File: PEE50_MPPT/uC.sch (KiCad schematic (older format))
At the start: 2 parts, among them U4 MSP430FR2353TDBT

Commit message: copy + pasten van schakeling
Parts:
- added J?: Conn_01x03_Female, symbol Connector:Conn_01x03_Female
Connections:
- net GND: now also J?.3 (Pin_3)
- net ADC: now reaches U4.7 (P1-0/UCB0STE/SMCLK/COMP0-0/A0/VEREF+)
- net at U4.8 (TEST/SBWTCK): now also J?.1 (Pin_1)
- net at U4.9 (*RST/NMI/SBWTDIO): now also J?.2 (Pin_2)
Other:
- note added: "RST\n"
- note added: "TEST"
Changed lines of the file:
@@
 $Descr A4 11693 8268
 encoding utf-8
-Sheet 3 5
+Sheet 3 11
 Title ""
 Date ""
@@
 Wire Wire Line
 	7700 4650 7500 4650
+$Comp
+L Connector:Conn_01x03_Female J?
+U 1 1 608C3F1C
+P 8800 2250
+F 0 "J?" H 8827 2276 50  0000 L CNN
+F 1 "Conn_01x03_Female" H 8827 2185 50  0000 L CNN
+F 2 "" H 8800 2250 50  0001 C CNN
+F 3 "~" H 8800 2250 50  0001 C CNN
+	1    8800 2250
+	1    0    0    -1
+$EndComp
+Wire Wire Line
+	7500 2150 8600 2150
+Wire Wire Line
+	8600 2250 7650 2250
+Wire Wire Line
+	7650 2250 7650 1950
+Wire Wire Line
+	7650 1950 3800 1950
+Wire Wire Line
+	3800 1950 3800 2150
+Wire Wire Line
+	3800 2150 3900 2150
+$Comp
+L power:GND #PWR?
+U 1 1 608C4239
+P 8550 2400
+F 0 "#PWR?" H 8550 2150 50  0001 C CNN
+F 1 "GND" H 8555 2227 50  0000 C CNN
+F 2 "" H 8550 2400 50  0001 C CNN
+F 3 "" H 8550 2400 50  0001 C CNN
+	1    8550 2400
+	1    0    0    -1
+$EndComp
+Wire Wire Line
+	8550 2400 8550 2350
+Wire Wire Line
+	8550 2350 8600 2350
+Text Notes 8300 2100 0    50   ~ 0
+TEST
+Text Notes 8300 2350 0    50   ~ 0
+RST\n
+Text HLabel 7650 2300 2    50   Input ~ 0
+ADC
+Wire Wire Line
+	7650 2300 7500 2300
 $EndSCHEMATC

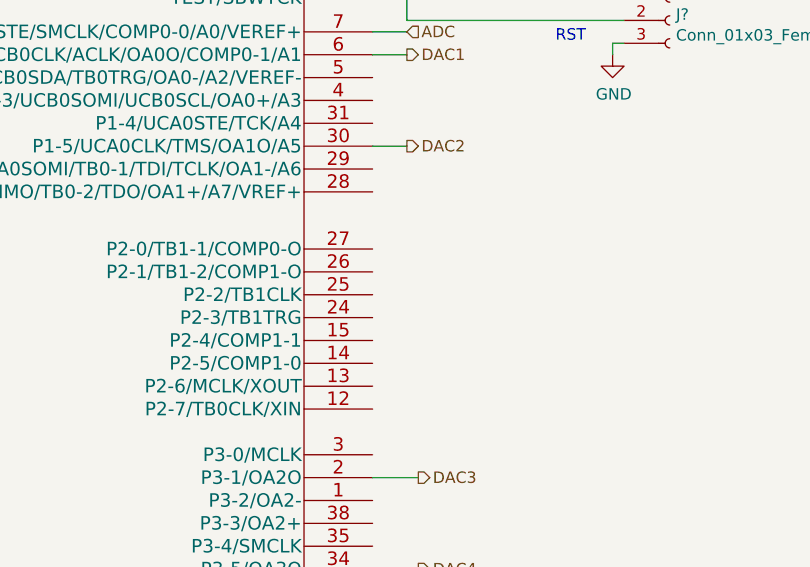
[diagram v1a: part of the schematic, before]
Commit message: mux ingevoegd en geintegreerd
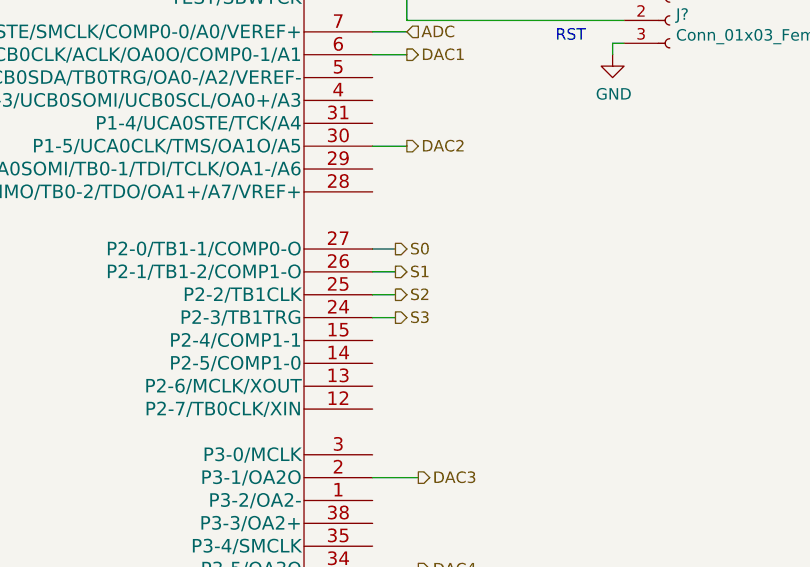
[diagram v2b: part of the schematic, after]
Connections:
- net S3: now reaches U4.24 (P2-3/TB1TRG)
- net S2: now reaches U4.25 (P2-2/TB1CLK)
- net S1: now reaches U4.26 (P2-1/TB1-2/COMP1-O)
- net S0: now reaches U4.27 (P2-0/TB1-1/COMP0-O)
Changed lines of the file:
@@
 $Descr A4 11693 8268
 encoding utf-8
-Sheet 3 11
+Sheet 3 15
 Title ""
 Date ""
@@
 	3800 2150 3900 2150
 $Comp
-L power:GND #PWR?
+L power:GND #PWR0133
 U 1 1 608C4239
 P 8550 2400
-F 0 "#PWR?" H 8550 2150 50  0001 C CNN
+F 0 "#PWR0133" H 8550 2150 50  0001 C CNN
 F 1 "GND" H 8555 2227 50  0000 C CNN
 F 2 "" H 8550 2400 50  0001 C CNN
@@
 Wire Wire Line
 	7650 2300 7500 2300
+Text HLabel 7600 3250 2    50   Output ~ 0
+S0
+Text HLabel 7600 3350 2    50   Output ~ 0
+S1
+Text HLabel 7600 3450 2    50   Output ~ 0
+S2
+Text HLabel 7600 3550 2    50   Output ~ 0
+S3
+Wire Wire Line
+	7500 3550 7600 3550
+Wire Wire Line
+	7500 3450 7600 3450
+Wire Wire Line
+	7500 3350 7600 3350
+Wire Wire Line
+	7500 3250 7600 3250
 $EndSCHEMATC

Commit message: schakeling klaar (denk ik)
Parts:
- added J7: Conn_01x02_Female, symbol Connector:Conn_01x02_Female
- gave numbers to parts that had none: 1
- renumbered C12 to C14, U4 to U5
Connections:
- net at U5.28 (P1-7/UCA0TXD/UCA0SIMO/TB0-2/TDO/OA1+/A7/VREF+): now also J7.2 (Pin_2)
- net at U5.29 (P1-6/UCA0RXD/UCA0SOMI/TB0-1/TDI/TCLK/OA1-/A6): now also J7.1 (Pin_1)
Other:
- note added: "uC RX\nuC TX\n"
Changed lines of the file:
@@
 $EndDescr
 $Comp
-L Robin_lib:MSP430FR2353TDBT U4
+L Robin_lib:MSP430FR2353TDBT U5
 U 1 1 608BCC4E
 P 5700 3600
-F 0 "U4" H 2650 4650 60  0000 C CNN
+F 0 "U5" H 2650 4650 60  0000 C CNN
 F 1 "MSP430FR2353TDBT" H 3050 4750 60  0000 C CNN
 F 2 "DBT38_TEX" H 4950 5250 60  0001 C CNN
@@
 $EndComp
 $Comp
-L power:GND #PWR0111
+L power:GND #PWR028
 U 1 1 608BCC99
 P 5700 5500
-F 0 "#PWR0111" H 5700 5250 50  0001 C CNN
+F 0 "#PWR028" H 5700 5250 50  0001 C CNN
 F 1 "GND" H 5705 5327 50  0000 C CNN
 F 2 "" H 5700 5500 50  0001 C CNN
@@
 	5700 5500 5700 5400
 $Comp
-L Device:C C12
+L Device:C C14
 U 1 1 608BF0BE
 P 5450 1650
-F 0 "C12" V 5198 1650 50  0000 C CNN
+F 0 "C14" V 5198 1650 50  0000 C CNN
 F 1 "C" V 5289 1650 50  0000 C CNN
 F 2 "" H 5488 1500 50  0001 C CNN
@@
 	5700 1650 5700 1800
 $Comp
-L power:GND #PWR0112
+L power:GND #PWR027
 U 1 1 608BF145
 P 5250 1650
-F 0 "#PWR0112" H 5250 1400 50  0001 C CNN
+F 0 "#PWR027" H 5250 1400 50  0001 C CNN
 F 1 "GND" V 5255 1522 50  0000 R CNN
 F 2 "" H 5250 1650 50  0001 C CNN
@@
 	7700 4650 7500 4650
 $Comp
-L Connector:Conn_01x03_Female J?
+L Connector:Conn_01x03_Female J8
 U 1 1 608C3F1C
 P 8800 2250
-F 0 "J?" H 8827 2276 50  0000 L CNN
+F 0 "J8" H 8827 2276 50  0000 L CNN
 F 1 "Conn_01x03_Female" H 8827 2185 50  0000 L CNN
 F 2 "" H 8800 2250 50  0001 C CNN
@@
 	3800 2150 3900 2150
 $Comp
-L power:GND #PWR0133
+L power:GND #PWR029
 U 1 1 608C4239
 P 8550 2400
-F 0 "#PWR0133" H 8550 2150 50  0001 C CNN
+F 0 "#PWR029" H 8550 2150 50  0001 C CNN
 F 1 "GND" H 8555 2227 50  0000 C CNN
 F 2 "" H 8550 2400 50  0001 C CNN
@@
 Wire Wire Line
 	7500 3250 7600 3250
+$Comp
+L Connector:Conn_01x02_Female J7
+U 1 1 6091D58E
+P 7800 2900
+F 0 "J7" H 7827 2876 50  0000 L CNN
+F 1 "Conn_01x02_Female" H 7827 2785 50  0000 L CNN
+F 2 "" H 7800 2900 50  0001 C CNN
+F 3 "~" H 7800 2900 50  0001 C CNN
+	1    7800 2900
+	1    0    0    -1
+$EndComp
+Wire Wire Line
+	7500 2900 7600 2900
+Wire Wire Line
+	7500 3000 7600 3000
+Text Notes 8000 3050 0    50   ~ 0
+uC RX\nuC TX\n
 $EndSCHEMATC

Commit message: best veel footprints ingevoegd
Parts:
- C14: footprint (none) -> Capacitor_SMD:C_1206_3216Metric_Pad1.42x1.75mm_HandSolder
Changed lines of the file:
@@
 EESchema Schematic File Version 4
-LIBS:PEE50_MPPT-cache
-EELAYER 26 0
+EELAYER 30 0
 EELAYER END
 $Descr A4 11693 8268
@@
 F 0 "C14" V 5198 1650 50  0000 C CNN
 F 1 "C" V 5289 1650 50  0000 C CNN
-F 2 "" H 5488 1500 50  0001 C CNN
+F 2 "Capacitor_SMD:C_1206_3216Metric_Pad1.42x1.75mm_HandSolder" H 5488 1500 50  0001 C CNN
 F 3 "~" H 5450 1650 50  0001 C CNN
 	1    5450 1650

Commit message: footprints gemapt + 10x10 pcb rand getekend
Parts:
- J7: footprint (none) -> Connector_PinSocket_2.54mm:PinSocket_1x02_P2.54mm_Vertical
- J8: footprint (none) -> Connector_PinSocket_2.54mm:PinSocket_1x03_P2.54mm_Vertical
- U5: footprint DBT38_TEX -> Robin_Lib:DBT38_TEX
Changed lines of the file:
@@
 EESchema Schematic File Version 4
-EELAYER 30 0
+LIBS:PEE50_MPPT-cache
+EELAYER 26 0
 EELAYER END
 $Descr A4 11693 8268
@@
 F 0 "U5" H 2650 4650 60  0000 C CNN
 F 1 "MSP430FR2353TDBT" H 3050 4750 60  0000 C CNN
-F 2 "DBT38_TEX" H 4950 5250 60  0001 C CNN
+F 2 "Robin_Lib:DBT38_TEX" H 4950 5250 60  0001 C CNN
 F 3 "" H 1600 4400 60  0000 C CNN
 	1    5700 3600
@@
 F 0 "J8" H 8827 2276 50  0000 L CNN
 F 1 "Conn_01x03_Female" H 8827 2185 50  0000 L CNN
-F 2 "" H 8800 2250 50  0001 C CNN
+F 2 "Connector_PinSocket_2.54mm:PinSocket_1x03_P2.54mm_Vertical" H 8800 2250 50  0001 C CNN
 F 3 "~" H 8800 2250 50  0001 C CNN
 	1    8800 2250
@@
 F 0 "J7" H 7827 2876 50  0000 L CNN
 F 1 "Conn_01x02_Female" H 7827 2785 50  0000 L CNN
-F 2 "" H 7800 2900 50  0001 C CNN
+F 2 "Connector_PinSocket_2.54mm:PinSocket_1x02_P2.54mm_Vertical" H 7800 2900 50  0001 C CNN
 F 3 "~" H 7800 2900 50  0001 C CNN
 	1    7800 2900

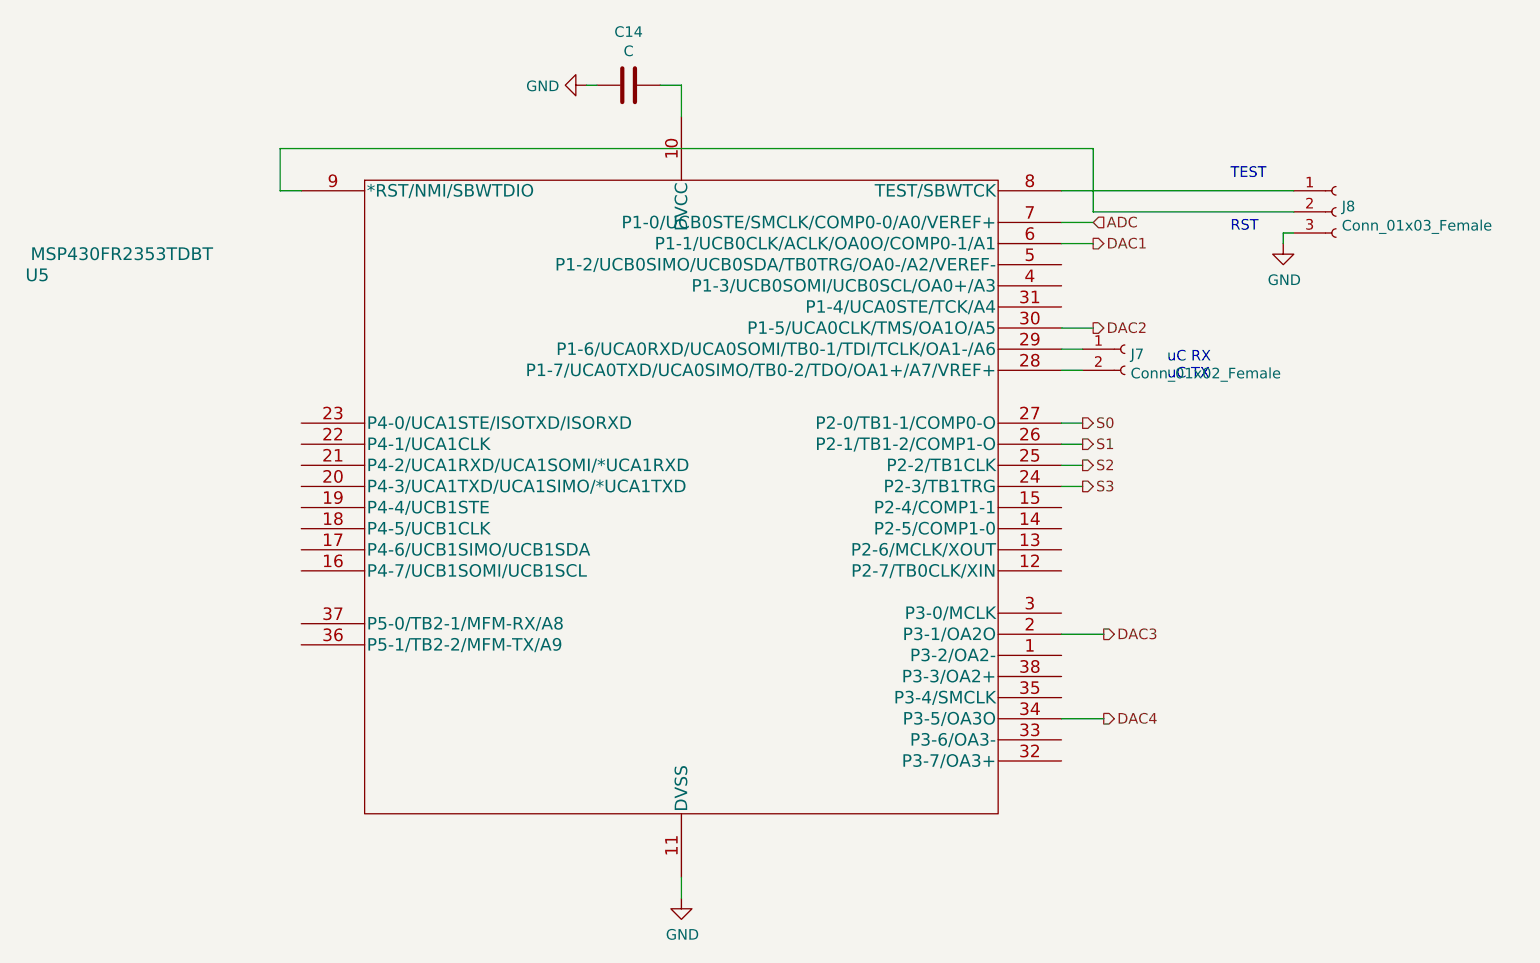
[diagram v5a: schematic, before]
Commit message: maar opnieuw begonnen met mppt layouten ivm plugin regels
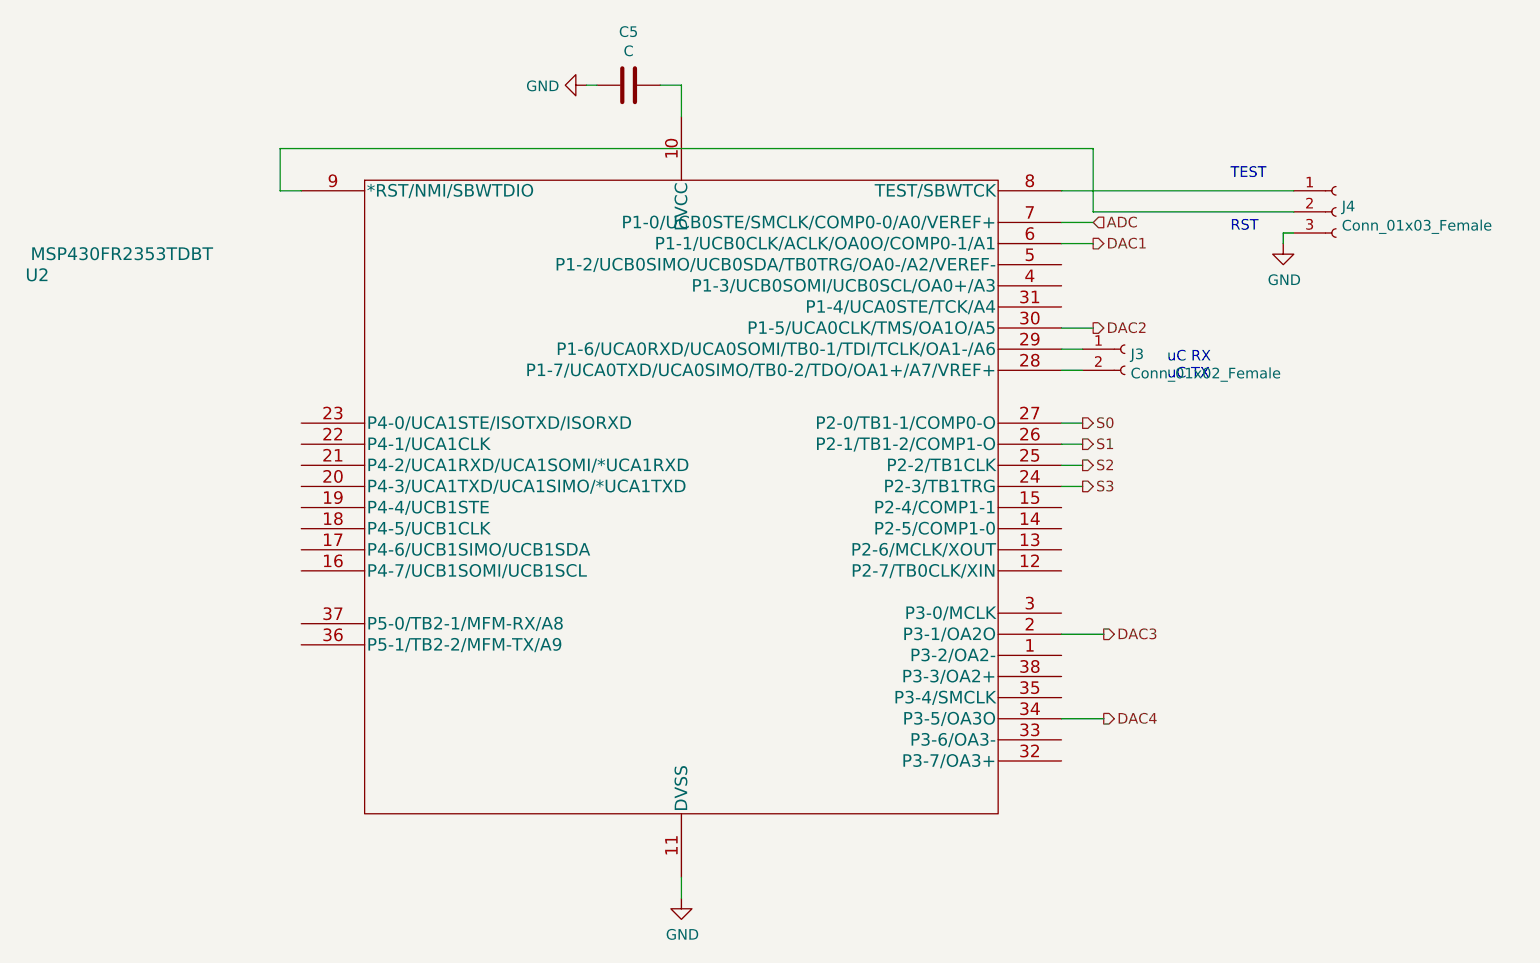
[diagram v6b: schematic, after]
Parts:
- renumbered C14 to C5, J7 to J3, J8 to J4, U5 to U2
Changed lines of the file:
@@
 $Descr A4 11693 8268
 encoding utf-8
-Sheet 3 15
+Sheet 3 19
 Title ""
 Date ""
@@
 $EndDescr
 $Comp
-L Robin_lib:MSP430FR2353TDBT U5
+L Robin_lib:MSP430FR2353TDBT U2
 U 1 1 608BCC4E
 P 5700 3600
-F 0 "U5" H 2650 4650 60  0000 C CNN
+F 0 "U2" H 2650 4650 60  0000 C CNN
 F 1 "MSP430FR2353TDBT" H 3050 4750 60  0000 C CNN
 F 2 "Robin_Lib:DBT38_TEX" H 4950 5250 60  0001 C CNN
@@
 $EndComp
 $Comp
-L power:GND #PWR028
+L power:GND #PWR010
 U 1 1 608BCC99
 P 5700 5500
-F 0 "#PWR028" H 5700 5250 50  0001 C CNN
+F 0 "#PWR010" H 5700 5250 50  0001 C CNN
 F 1 "GND" H 5705 5327 50  0000 C CNN
 F 2 "" H 5700 5500 50  0001 C CNN
@@
 	5700 5500 5700 5400
 $Comp
-L Device:C C14
+L Device:C C5
 U 1 1 608BF0BE
 P 5450 1650
-F 0 "C14" V 5198 1650 50  0000 C CNN
+F 0 "C5" V 5198 1650 50  0000 C CNN
 F 1 "C" V 5289 1650 50  0000 C CNN
 F 2 "Capacitor_SMD:C_1206_3216Metric_Pad1.42x1.75mm_HandSolder" H 5488 1500 50  0001 C CNN
@@
 	5700 1650 5700 1800
 $Comp
-L power:GND #PWR027
+L power:GND #PWR09
 U 1 1 608BF145
 P 5250 1650
-F 0 "#PWR027" H 5250 1400 50  0001 C CNN
+F 0 "#PWR09" H 5250 1400 50  0001 C CNN
 F 1 "GND" V 5255 1522 50  0000 R CNN
 F 2 "" H 5250 1650 50  0001 C CNN
@@
 	7700 4650 7500 4650
 $Comp
-L Connector:Conn_01x03_Female J8
+L Connector:Conn_01x03_Female J4
 U 1 1 608C3F1C
 P 8800 2250
-F 0 "J8" H 8827 2276 50  0000 L CNN
+F 0 "J4" H 8827 2276 50  0000 L CNN
 F 1 "Conn_01x03_Female" H 8827 2185 50  0000 L CNN
 F 2 "Connector_PinSocket_2.54mm:PinSocket_1x03_P2.54mm_Vertical" H 8800 2250 50  0001 C CNN
@@
 	3800 2150 3900 2150
 $Comp
-L power:GND #PWR029
+L power:GND #PWR011
 U 1 1 608C4239
 P 8550 2400
-F 0 "#PWR029" H 8550 2150 50  0001 C CNN
+F 0 "#PWR011" H 8550 2150 50  0001 C CNN
 F 1 "GND" H 8555 2227 50  0000 C CNN
 F 2 "" H 8550 2400 50  0001 C CNN
@@
 	7500 3250 7600 3250
 $Comp
-L Connector:Conn_01x02_Female J7
+L Connector:Conn_01x02_Female J3
 U 1 1 6091D58E
 P 7800 2900
-F 0 "J7" H 7827 2876 50  0000 L CNN
+F 0 "J3" H 7827 2876 50  0000 L CNN
 F 1 "Conn_01x02_Female" H 7827 2785 50  0000 L CNN
 F 2 "Connector_PinSocket_2.54mm:PinSocket_1x02_P2.54mm_Vertical" H 7800 2900 50  0001 C CNN

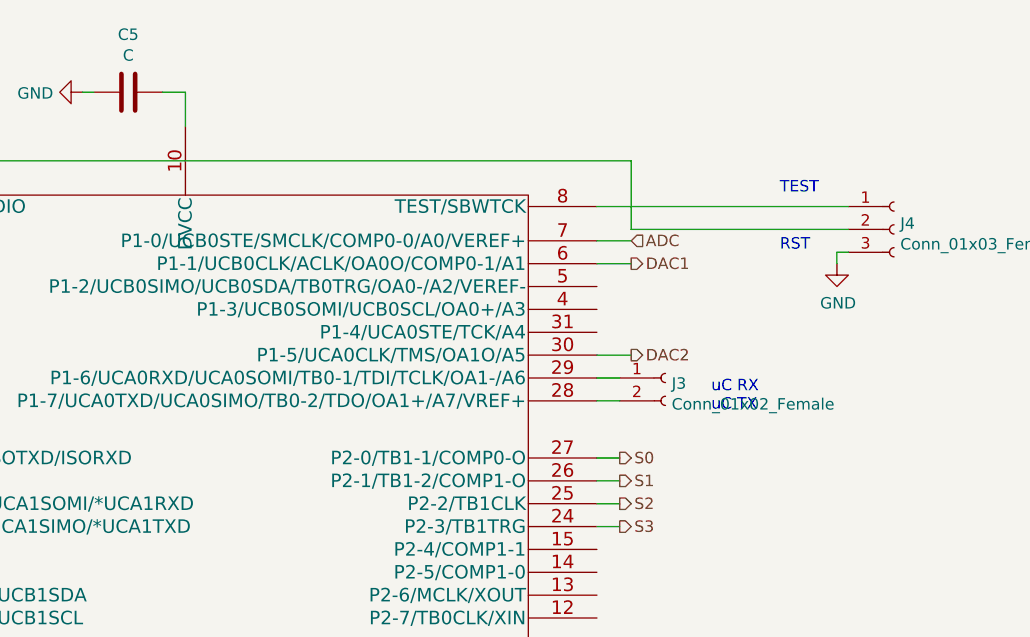
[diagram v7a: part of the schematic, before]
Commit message: spinneweb aangemaakt
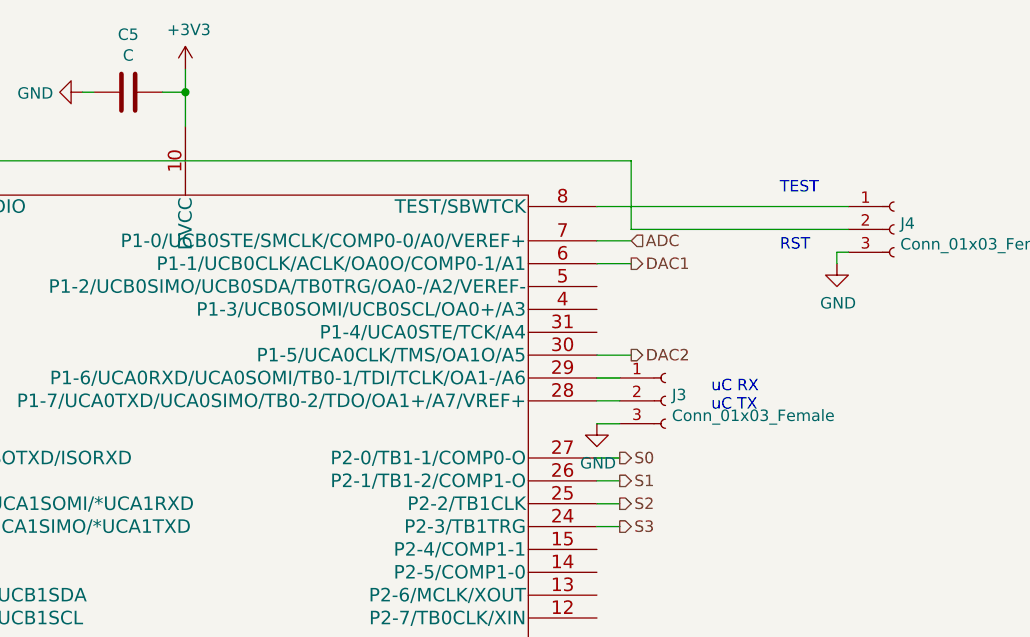
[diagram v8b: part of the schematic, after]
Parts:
- removed J3: Conn_01x02_Female, Connector_PinSocket_2.54mm:PinSocket_1x02_P2.54mm_Vertical, symbol Connector:Conn_01x02_Female
- added J3: Conn_01x03_Female, Connector_PinSocket_2.54mm:PinSocket_1x03_P2.54mm_Vertical, symbol Connector:Conn_01x03_Female
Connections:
- net GND: now also J3.3 (Pin_3)
- net +3V3: now reaches C5.1, U2.10 (DVCC)
- net at U2.28 (P1-7/UCA0TXD/UCA0SIMO/TB0-2/TDO/OA1+/A7/VREF+): now also J3.2 (Pin_2)
- net at U2.29 (P1-6/UCA0RXD/UCA0SOMI/TB0-1/TDI/TCLK/OA1-/A6): now also J3.1 (Pin_1)
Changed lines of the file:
@@
 Wire Wire Line
 	7500 3250 7600 3250
-$Comp
-L Connector:Conn_01x02_Female J3
-U 1 1 6091D58E
-P 7800 2900
-F 0 "J3" H 7827 2876 50  0000 L CNN
-F 1 "Conn_01x02_Female" H 7827 2785 50  0000 L CNN
-F 2 "Connector_PinSocket_2.54mm:PinSocket_1x02_P2.54mm_Vertical" H 7800 2900 50  0001 C CNN
-F 3 "~" H 7800 2900 50  0001 C CNN
-	1    7800 2900
-	1    0    0    -1
-$EndComp
 Wire Wire Line
 	7500 2900 7600 2900
@@
 Text Notes 8000 3050 0    50   ~ 0
 uC RX\nuC TX\n
+$Comp
+L power:+3V3 #PWR0101
+U 1 1 609D348B
+P 5700 1550
+F 0 "#PWR0101" H 5700 1400 50  0001 C CNN
+F 1 "+3V3" H 5715 1723 50  0000 C CNN
+F 2 "" H 5700 1550 50  0001 C CNN
+F 3 "" H 5700 1550 50  0001 C CNN
+	1    5700 1550
+	1    0    0    -1
+$EndComp
+Wire Wire Line
+	5700 1550 5700 1650
+Connection ~ 5700 1650
+$Comp
+L Connector:Conn_01x03_Female J3
+U 1 1 609DA506
+P 7800 3000
+F 0 "J3" H 7828 3026 50  0000 L CNN
+F 1 "Conn_01x03_Female" H 7828 2935 50  0000 L CNN
+F 2 "Connector_PinSocket_2.54mm:PinSocket_1x03_P2.54mm_Vertical" H 7800 3000 50  0001 C CNN
+F 3 "~" H 7800 3000 50  0001 C CNN
+	1    7800 3000
+	1    0    0    -1
+$EndComp
+$Comp
+L power:GND #PWR0102
+U 1 1 609DACF1
+P 7500 3100
+F 0 "#PWR0102" H 7500 2850 50  0001 C CNN
+F 1 "GND" H 7505 2927 50  0000 C CNN
+F 2 "" H 7500 3100 50  0001 C CNN
+F 3 "" H 7500 3100 50  0001 C CNN
+	1    7500 3100
+	1    0    0    -1
+$EndComp
+Wire Wire Line
+	7500 3100 7600 3100
 $EndSCHEMATC
